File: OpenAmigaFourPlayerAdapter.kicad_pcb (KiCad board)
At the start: 2 copper layers, 64.4 x 26.5 mm, 6 parts, among them J1 F25HP, J3 F09HP, J4 F09HP, J99 OSHW_LOGO

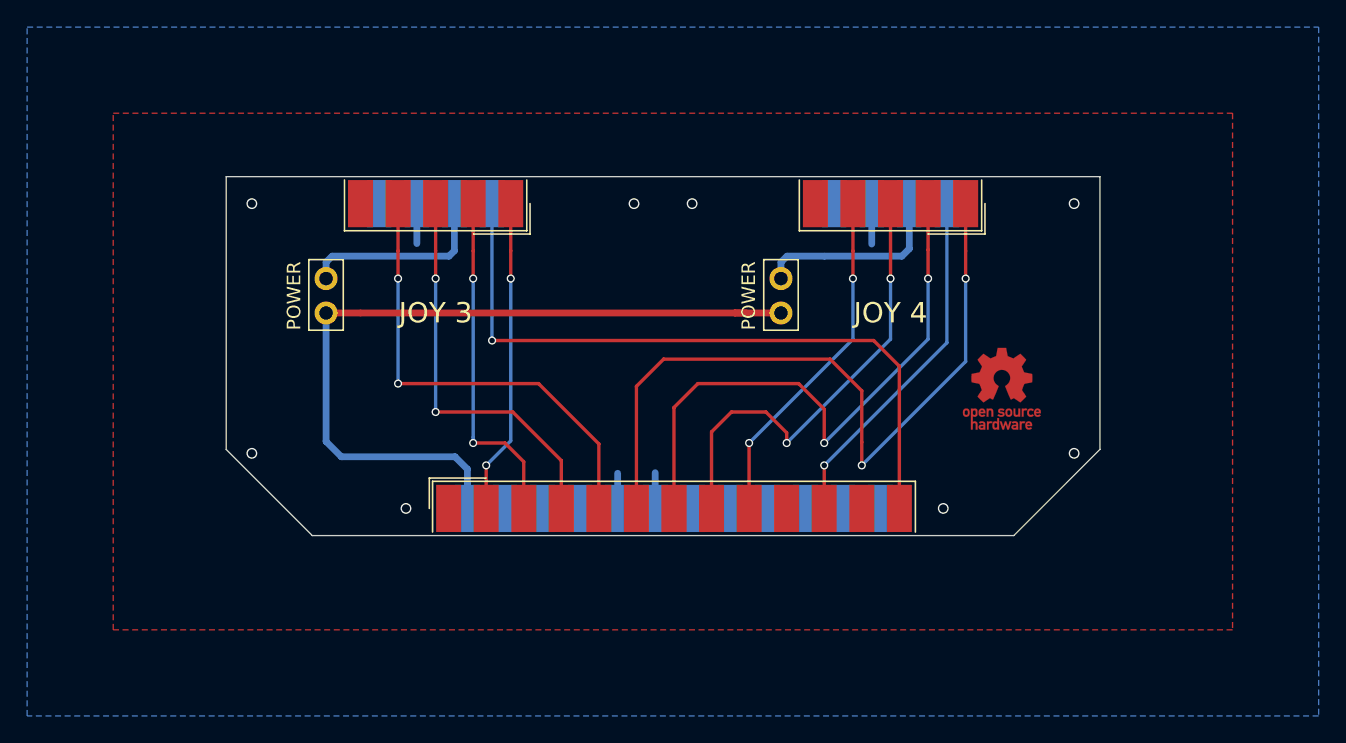
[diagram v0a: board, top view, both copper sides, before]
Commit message: Change shape so that we don't bump in audio connectors on A600/A1200
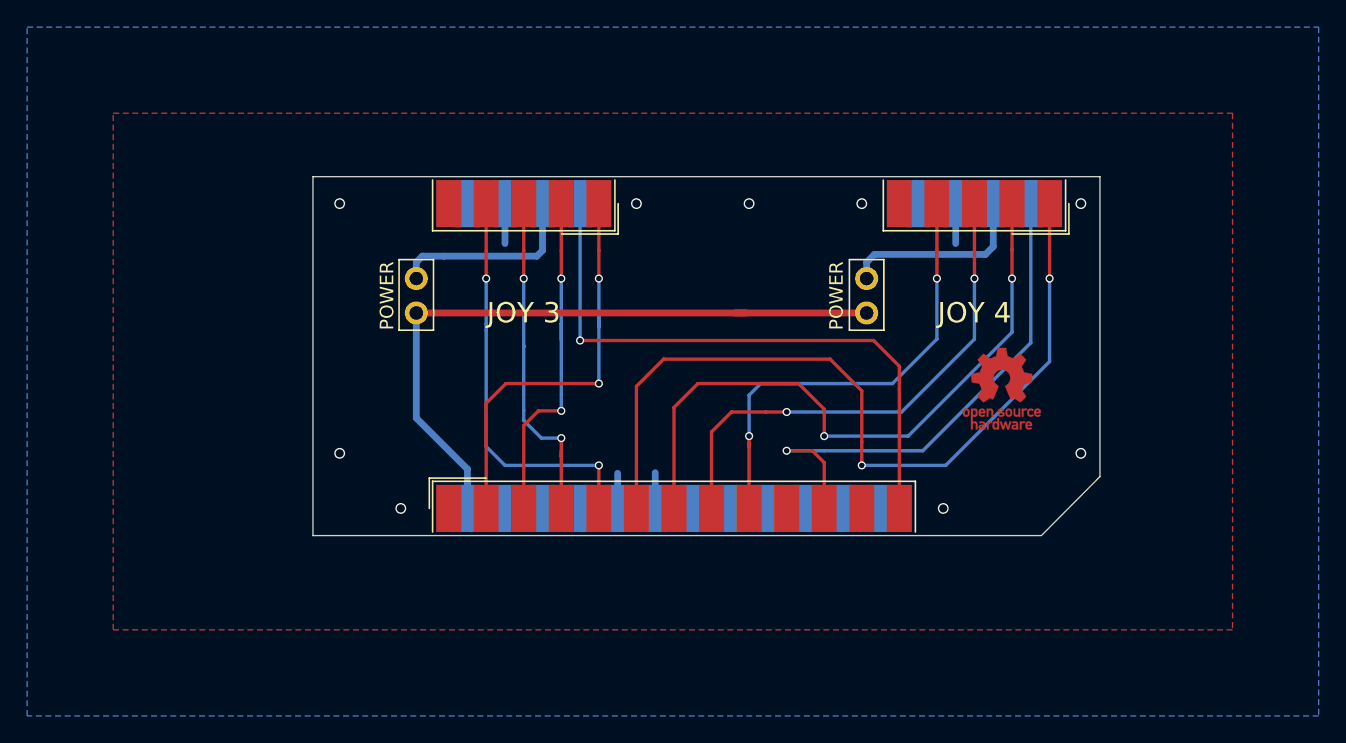
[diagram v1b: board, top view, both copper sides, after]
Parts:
- moved JP3 6.66 mm to (130.3, 94.7)
- moved J3 6.50 mm to (138.2, 89.2)
- moved JP4 6.32 mm to (163.5, 94.7)
- moved J4 6.19 mm to (171.5, 89.2)
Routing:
- net /fire4: track 26.2 -> 38.1 mm
- net /right4: track 25.7 -> 34.2 mm
- net /+5v: track 58.0 -> 50.0 mm
- net /up3: track 23.2 -> 30.7 mm
- net /fire3: track 51.4 -> 44.9 mm
- net /up4: track 55.4 -> 61.6 mm
- net /down4: track 43.4 -> 48.5 mm
- net /left3: track 29.7 -> 24.9 mm
- net /right3: track 34.7 -> 30.0 mm
- net /left4: track 34.0 -> 37.9 mm
- net /gnd: track 11.2 -> 11.1 mm, vias 8 -> 9
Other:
- board size 64.4 x 26.5 mm -> 58 x 26.5 mm
- board text added: "V2"
- board text removed: "V1"

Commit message: Fix board outline
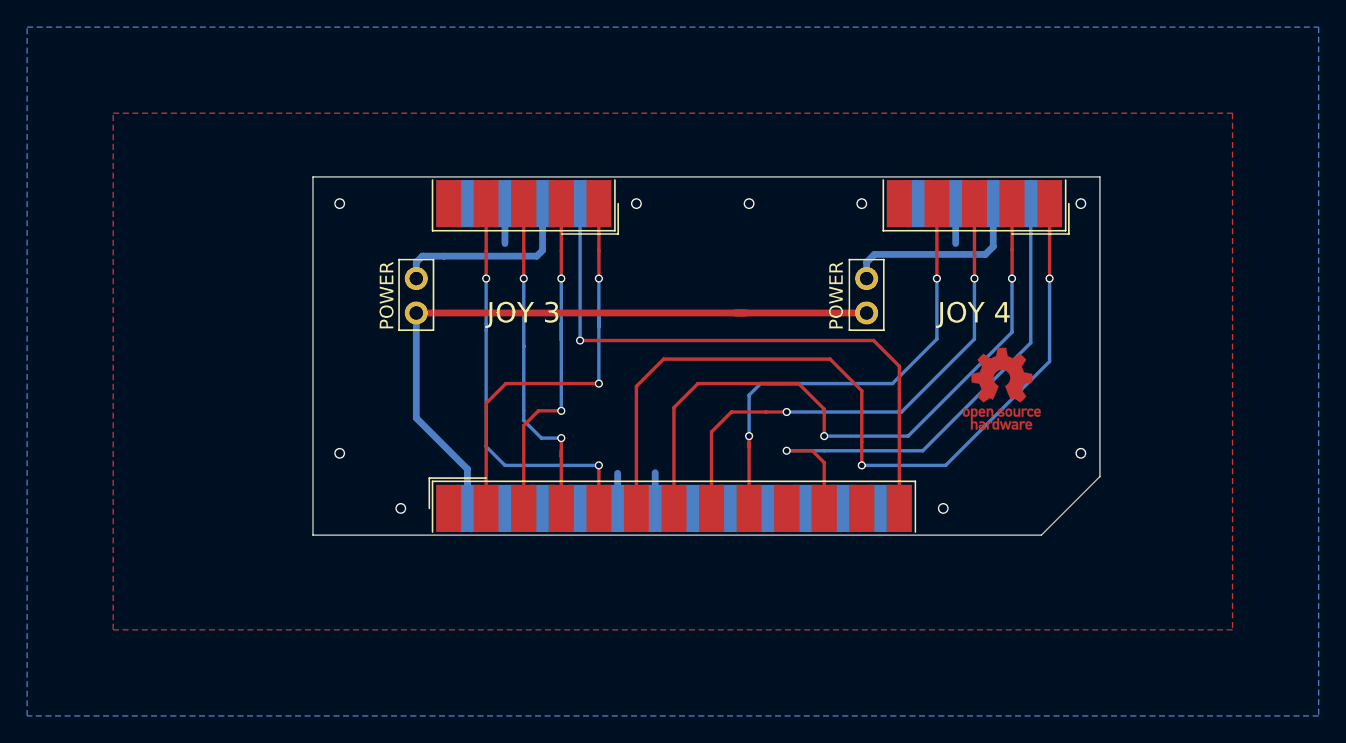
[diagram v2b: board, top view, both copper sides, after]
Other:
- board size 58 x 26.5 mm -> 58 x 26.4 mm
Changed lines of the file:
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@@
       (xy 0.376964 -2.709982)) (layer Top) (width 0.01))
   )
-  (gr_line (start 176.403 113.6981) (end 180.721 109.347) (layer Edge.Cuts) (width 0.05))
+  (gr_line (start 176.403 113.665) (end 180.721 109.347) (layer Edge.Cuts) (width 0.05))
   (gr_text "github.com/SukkoPera/OpenAmigaFourPlayerAdapter\n\nLicensed under CERN OHL v.1.2" (at 151.701499 102.362) (layer B.SilkS)
     (effects (font (size 1 1) (thickness 0.15)) (justify mirror))
@@
     (effects (font (size 1.5 1.5) (thickness 0.3)))
   )
-  (gr_line (start 122.682 87.2286) (end 122.682 113.6981) (layer Edge.Cuts) (width 0.05))
-  (gr_line (start 122.682 113.6981) (end 176.403 113.6981) (layer Edge.Cuts) (width 0.05))
-  (gr_line (start 180.721 109.347) (end 180.721 87.2286) (layer Edge.Cuts) (width 0.05))
-  (gr_line (start 180.721 87.2286) (end 122.682 87.2286) (layer Edge.Cuts) (width 0.05))
+  (gr_line (start 122.682 87.249) (end 122.682 113.665) (layer Edge.Cuts) (width 0.05))
+  (gr_line (start 122.682 113.665) (end 176.403 113.665) (layer Edge.Cuts) (width 0.05))
+  (gr_line (start 180.721 109.347) (end 180.721 87.249) (layer Edge.Cuts) (width 0.05))
+  (gr_line (start 180.721 87.249) (end 122.682 87.249) (layer Edge.Cuts) (width 0.05))
   (segment (start 130.750919 93.091) (end 130.81 93.091) (width 0.5) (layer Bottom) (net 1))
   (segment (start 130.302 93.539919) (end 130.750919 93.091) (width 0.5) (layer Bottom) (net 1))

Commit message: Make board slightly shorter
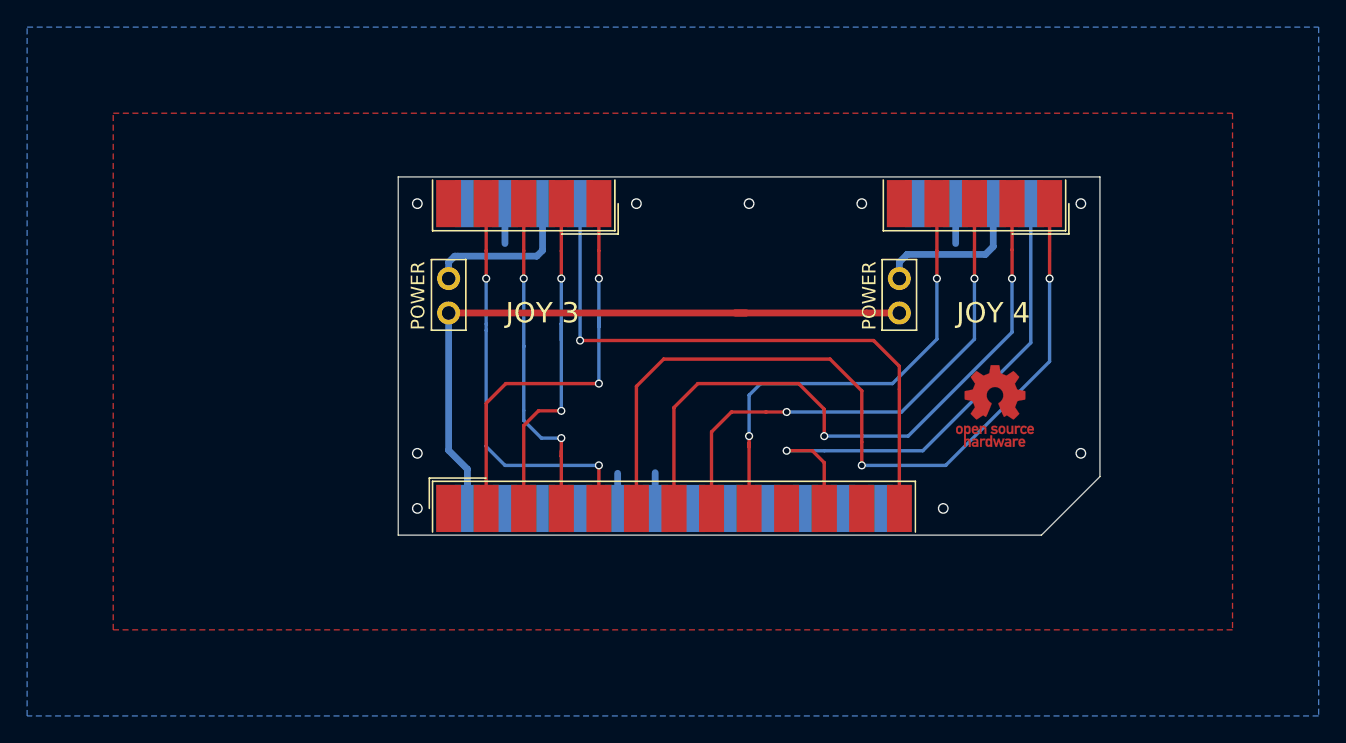
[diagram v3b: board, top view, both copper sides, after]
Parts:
- moved JP4 2.41 mm to (165.9, 94.7)
- moved JP3 2.38 mm to (132.7, 94.7)
- moved J99 1.37 mm to (173.0, 104.1)
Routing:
- net Net-(J4-Pad7): track 14.2 -> 11.8 mm
- net Net-(J3-Pad7): track 14.3 -> 11.9 mm
- net /+5v: track 50.0 -> 49.1 mm
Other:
- board size 58 x 26.4 mm -> 51.8 x 26.4 mm
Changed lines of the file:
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@@
     (thickness 1.6)
     (drawings 11)
-    (tracks 138)
+    (tracks 139)
     (zones 0)
     (modules 6)
@@
   )
   (module OpenAmigaFourPlayerAdapter:PinHeader_1x02_P2.54mm_Vertical (layer Top)
-    (at 130.302 94.742)
+    (at 132.6855 94.742)
     (descr "Through hole straight pin header, 1x02, 2.54mm pitch, single row")
     (tags "Through hole pin header THT 1x02 2.54mm single row")
@@
   )
   (module OpenAmigaFourPlayerAdapter:PinHeader_1x02_P2.54mm_Vertical (layer Top)
-    (at 163.5125 94.742)
+    (at 165.9255 94.742)
     (descr "Through hole straight pin header, 1x02, 2.54mm pitch, single row")
     (tags "Through hole pin header THT 1x02 2.54mm single row")
@@
   )
   (module Symbol:OSHW-Logo_5.7x6mm_Copper (layer Top)
-    (at 173.482 102.87)
+    (at 172.974 104.14)
     (descr "Open Source Hardware Logo")
     (tags "Logo OSHW")
@@
   )
   (gr_line (start 176.403 113.665) (end 180.721 109.347) (layer Edge.Cuts) (width 0.05))
-  (gr_text "github.com/SukkoPera/OpenAmigaFourPlayerAdapter\n\nLicensed under CERN OHL v.1.2" (at 151.701499 102.362) (layer B.SilkS)
+  (gr_text "github.com/SukkoPera/OpenAmigaFourPlayerAdapter\n\nLicensed under CERN OHL v.1.2" (at 154.844749 102.362) (layer B.SilkS)
     (effects (font (size 1 1) (thickness 0.15)) (justify mirror))
   )
-  (gr_text V2 (at 124.46 112.395) (layer B.SilkS)
+  (gr_text V2 (at 175.514 112.268) (layer B.SilkS)
     (effects (font (size 1 1) (thickness 0.15)) (justify mirror))
   )
-  (gr_text POWER (at 161.29 96.012 90) (layer F.SilkS)
+  (gr_text POWER (at 163.703 96.012 90) (layer F.SilkS)
     (effects (font (size 1 1) (thickness 0.15)))
   )
-  (gr_text POWER (at 128.143 96.012 90) (layer F.SilkS)
+  (gr_text POWER (at 130.429 96.012 90) (layer F.SilkS)
     (effects (font (size 1 1) (thickness 0.15)))
   )
-  (gr_text "JOY 4" (at 171.4655 97.282) (layer F.SilkS)
+  (gr_text "JOY 4" (at 172.8505 97.282) (layer F.SilkS)
     (effects (font (size 1.5 1.5) (thickness 0.3)))
   )
-  (gr_text "JOY 3" (at 138.2255 97.282) (layer F.SilkS)
+  (gr_text "JOY 3" (at 139.6105 97.282) (layer F.SilkS)
     (effects (font (size 1.5 1.5) (thickness 0.3)))
   )
-  (gr_line (start 122.682 87.249) (end 122.682 113.665) (layer Edge.Cuts) (width 0.05))
-  (gr_line (start 122.682 113.665) (end 176.403 113.665) (layer Edge.Cuts) (width 0.05))
+  (gr_line (start 128.9685 87.249) (end 128.9685 113.665) (layer Edge.Cuts) (width 0.05))
+  (gr_line (start 128.9685 113.665) (end 176.403 113.665) (layer Edge.Cuts) (width 0.05))
   (gr_line (start 180.721 109.347) (end 180.721 87.249) (layer Edge.Cuts) (width 0.05))
-  (gr_line (start 180.721 87.249) (end 122.682 87.249) (layer Edge.Cuts) (width 0.05))
-  (segment (start 130.750919 93.091) (end 130.81 93.091) (width 0.5) (layer Bottom) (net 1))
-  (segment (start 130.302 93.539919) (end 130.750919 93.091) (width 0.5) (layer Bottom) (net 1))
-  (segment (start 130.302 94.742) (end 130.302 93.539919) (width 0.5) (layer Bottom) (net 1))
+  (gr_line (start 180.721 87.249) (end 128.9685 87.249) (layer Edge.Cuts) (width 0.05))
   (segment (start 139.6105 89.2175) (end 139.6105 92.6725) (width 0.5) (layer Bottom) (net 1))
-  (segment (start 139.192 93.091) (end 132.334 93.091) (width 0.5) (layer Bottom) (net 1))
   (segment (start 139.6105 92.6725) (end 139.192 93.091) (width 0.5) (layer Bottom) (net 1))
-  (segment (start 130.81 93.091) (end 132.334 93.091) (width 0.5) (layer Bottom) (net 1))
-  (segment (start 163.5125 93.539919) (end 163.5125 94.742) (width 0.5) (layer Bottom) (net 2))
-  (segment (start 164.088419 92.964) (end 163.5125 93.539919) (width 0.5) (layer Bottom) (net 2))
-  (segment (start 172.2755 92.964) (end 164.088419 92.964) (width 0.5) (layer Bottom) (net 2))
+  (segment (start 133.134419 93.091) (end 133.35 93.091) (width 0.5) (layer Bottom) (net 1))
+  (segment (start 132.6855 94.742) (end 132.6855 93.539919) (width 0.5) (layer Bottom) (net 1))
+  (segment (start 139.192 93.091) (end 133.35 93.091) (width 0.5) (layer Bottom) (net 1))
+  (segment (start 132.6855 93.539919) (end 133.134419 93.091) (width 0.5) (layer Bottom) (net 1))
   (segment (start 172.8505 92.389) (end 172.2755 92.964) (width 0.5) (layer Bottom) (net 2))
   (segment (start 172.8505 89.2175) (end 172.8505 92.389) (width 0.5) (layer Bottom) (net 2))
+  (segment (start 166.497 92.968419) (end 166.497 92.964) (width 0.5) (layer Bottom) (net 2))
+  (segment (start 165.9255 93.539919) (end 166.497 92.968419) (width 0.5) (layer Bottom) (net 2))
+  (segment (start 165.9255 94.742) (end 165.9255 93.539919) (width 0.5) (layer Bottom) (net 2))
+  (segment (start 172.2755 92.964) (end 166.497 92.964) (width 0.5) (layer Bottom) (net 2))
   (via (at 143.7655 94.742) (size 0.6) (drill 0.4) (layers Top Bottom) (net 3))
   (segment (start 143.7655 92.6895) (end 143.7655 94.742) (width 0.25) (layer Top) (net 3))
@@
   (segment (start 134.0705 108.7975) (end 134.0705 109.8135) (width 0.5) (layer Bottom) (net 12))
   (segment (start 154.655 97.282) (end 153.797 97.282) (width 0.5) (layer Top) (net 12))
-  (segment (start 130.302 105.029) (end 134.0705 108.7975) (width 0.5) (layer Bottom) (net 12))
-  (segment (start 130.302 97.282) (end 130.302 105.029) (width 0.5) (layer Bottom) (net 12))
-  (segment (start 130.302 97.282) (end 163.5125 97.282) (width 0.5) (layer Top) (net 12))
+  (segment (start 132.6855 107.4125) (end 134.0705 108.7975) (width 0.5) (layer Bottom) (net 12))
+  (segment (start 132.6855 97.282) (end 132.6855 107.4125) (width 0.5) (layer Bottom) (net 12))
+  (segment (start 163.5125 97.282) (end 165.9255 97.282) (width 0.5) (layer Top) (net 12))
+  (segment (start 132.6855 97.282) (end 163.5125 97.282) (width 0.5) (layer Top) (net 12))
   (segment (start 136.8405 89.2175) (end 136.8405 92.1625) (width 0.5) (layer Bottom) (net 13) (status 10))
-  (via (at 124.6505 89.2175) (size 0.8) (drill 0.6) (layers Top Bottom) (net 13))
+  (via (at 130.377833 89.2175) (size 0.8) (drill 0.6) (layers Top Bottom) (net 13))
   (segment (start 147.9205 111.6965) (end 147.9205 109.0585) (width 0.5) (layer Bottom) (net 13) (status 10))
   (segment (start 145.1505 111.6965) (end 145.1505 109.1035) (width 0.5) (layer Bottom) (net 13) (status 10))
   (via (at 179.312415 89.2175) (size 0.8) (drill 0.6) (layers Top Bottom) (net 13))
-  (via (at 124.6505 107.6325) (size 0.8) (drill 0.6) (layers Top Bottom) (net 13))
+  (via (at 130.377833 107.6325) (size 0.8) (drill 0.6) (layers Top Bottom) (net 13))
   (via (at 179.312415 107.6325) (size 0.8) (drill 0.6) (layers Top Bottom) (net 13))
-  (via (at 129.159 111.6965) (size 0.8) (drill 0.6) (layers Top Bottom) (net 13))
+  (via (at 130.377833 111.6965) (size 0.8) (drill 0.6) (layers Top Bottom) (net 13))
   (via (at 169.164 111.6965) (size 0.8) (drill 0.6) (layers Top Bottom) (net 13))
   (via (at 154.8455 89.2175) (size 0.8) (drill 0.6) (layers Top Bottom) (net 13))
